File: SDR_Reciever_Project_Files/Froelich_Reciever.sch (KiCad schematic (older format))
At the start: 84 parts, among them J1 I_IN0, J10 LO_I, J11 4.3V, J12 CLK0, J13 RF_IN, J14 RF_OUT, J15 Antenna In, J16 CLK1, J17 CLK2, J18 Conn_01x02_Female, J19 Conn_01x02_Female, J2 I_AMP, J20 I_OUT, J21 Q_OUT, J3 I_IN180, J4 AudioJack3, J5 Q_IN90, J6 Q_AMP, J7 Q_IN270, J8 LO_Q, J9 5V, Q1 PN2222A, U1 INA821ID, U2 SN74CBT3253, U3 OP213FPZ, U4 INA821ID, U5 74AC74, U6 Si5351A-B-GT, U7 LM741, Y1 ATS250

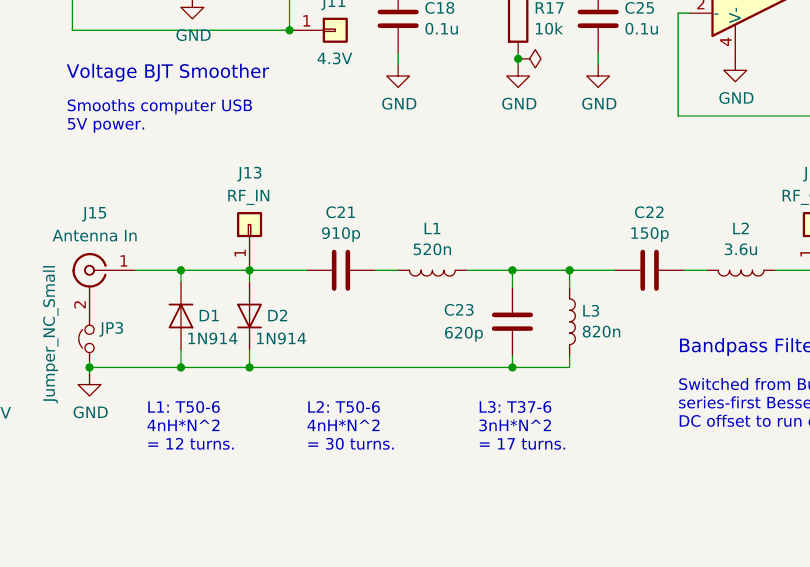
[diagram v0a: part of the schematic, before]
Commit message: Updates to v3a schematics and a few images added.
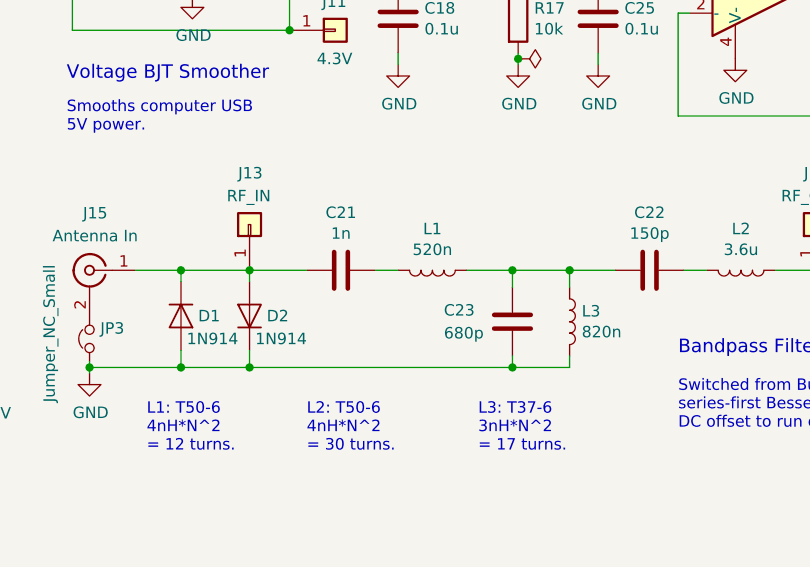
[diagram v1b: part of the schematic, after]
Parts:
- C21: value 910p -> 1n
- C23: value 620p -> 680p
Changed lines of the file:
@@
 P 8125 5600
 F 0 "C21" V 7873 5600 50  0000 C CNN
-F 1 "910p" V 7964 5600 50  0000 C CNN
+F 1 "1n" V 7964 5600 50  0000 C CNN
 F 2 "Capacitor_THT:C_Disc_D5.0mm_W2.5mm_P2.50mm" H 8163 5450 50  0001 C CNN
 F 3 "~" H 8125 5600 50  0001 C CNN
@@
 P 8875 5825
 F 0 "C23" H 8575 5875 50  0000 L CNN
-F 1 "620p" H 8575 5775 50  0000 L CNN
+F 1 "680p" H 8575 5775 50  0000 L CNN
 F 2 "Capacitor_THT:C_Disc_D4.7mm_W2.5mm_P5.00mm" H 8913 5675 50  0001 C CNN
 F 3 "~" H 8875 5825 50  0001 C CNN
